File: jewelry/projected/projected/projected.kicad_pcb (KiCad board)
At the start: 2 copper layers, 28 x 28 mm, 29 parts, among them J4 Leds, U1 STM32F042K6U6, U2 MCP73812T-420I-OT, U3 PCA9306DCUR, U4 MCP1640BCH

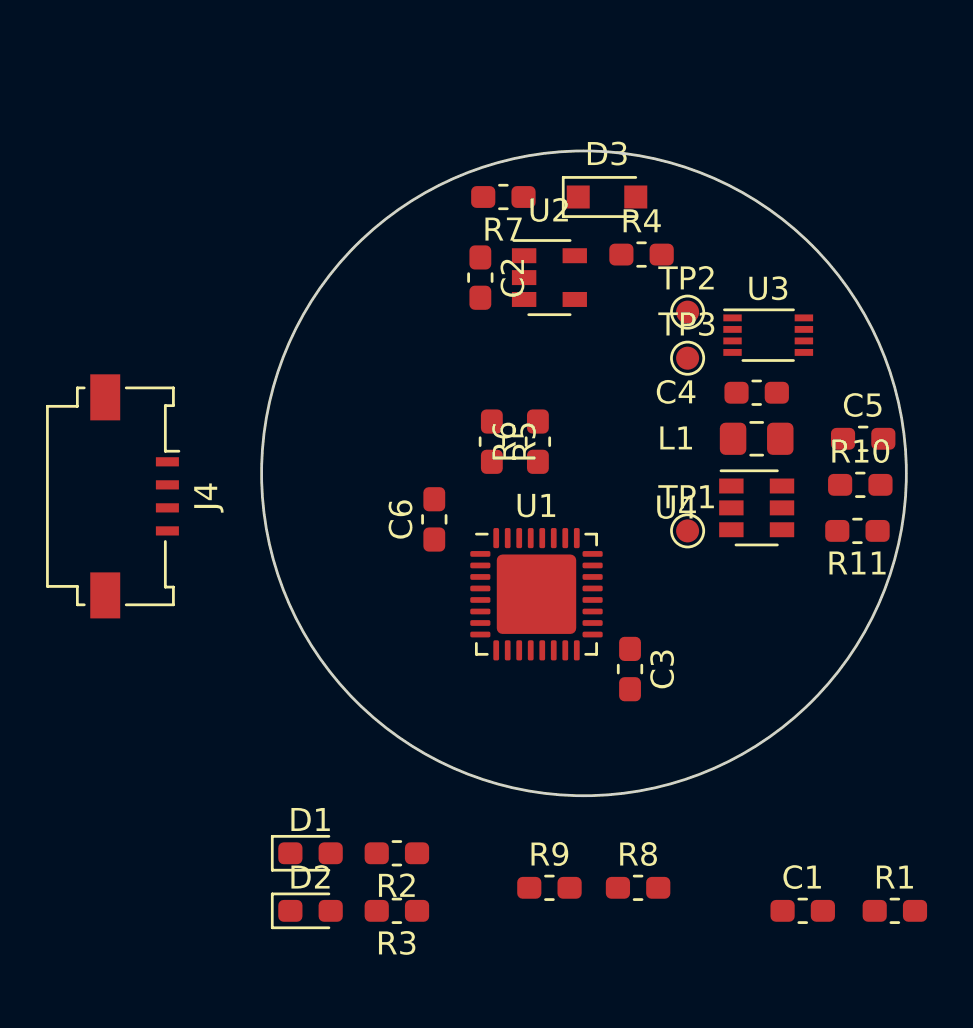
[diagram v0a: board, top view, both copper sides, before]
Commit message: projected: Try to fit accelerometer and mic
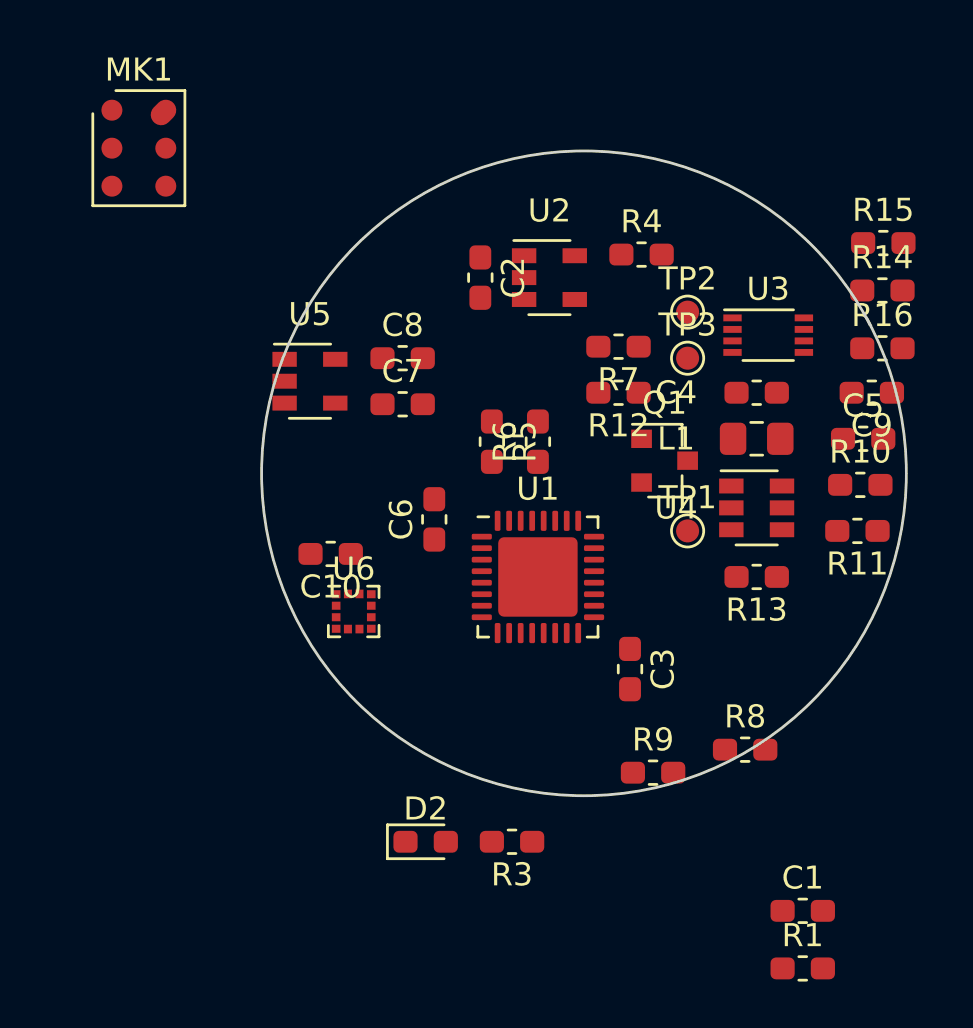
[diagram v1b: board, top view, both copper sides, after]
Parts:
- removed D1: LED, LED_SMD:LED_0603_1608Metric_Pad1.05x0.95mm_HandSolder
- removed D3: Z3V9, Diode_SMD:D_SOD-323_HandSoldering
- removed J4: Leds, Connector_FFC-FPC:Molex_200528-0040_1x04-1MP_P1.00mm_Horizontal
- removed R2: R, Resistor_SMD:R_0603_1608Metric_Pad1.05x0.95mm_HandSolder
- added C10: 1uF, Capacitor_SMD:C_0603_1608Metric_Pad1.05x0.95mm_HandSolder, F.Cu at (39.0, 53.5)
- added C7: 1uF, Capacitor_SMD:C_0603_1608Metric_Pad1.05x0.95mm_HandSolder, F.Cu at (42.1, 47.0)
- added C8: 1uF, Capacitor_SMD:C_0603_1608Metric_Pad1.05x0.95mm_HandSolder, F.Cu at (42.1, 45.0)
- added C9: 1uF, Capacitor_SMD:C_0603_1608Metric_Pad1.05x0.95mm_HandSolder, F.Cu at (62.5, 46.5)
- added MK1: MP45DT02, Sensor_Audio:ST_HLGA-6_3.76x4.72mm_P1.65mm, F.Cu at (30.7, 35.9)
- added Q1: BC847, Package_TO_SOT_SMD:SOT-23, F.Cu at (53.5, 49.5)
- added R12: 4k7, Resistor_SMD:R_0603_1608Metric_Pad1.05x0.95mm_HandSolder, F.Cu at (51.5, 46.5)
- added R13: 100k, Resistor_SMD:R_0603_1608Metric_Pad1.05x0.95mm_HandSolder, F.Cu at (57.5, 54.5)
- added R14: 100k, Resistor_SMD:R_0603_1608Metric_Pad1.05x0.95mm_HandSolder, F.Cu at (63.0, 42.1)
- added R15: 3k3, Resistor_SMD:R_0603_1608Metric_Pad1.05x0.95mm_HandSolder, F.Cu at (63.0, 40.0)
- added R16: 3k3, Resistor_SMD:R_0603_1608Metric_Pad1.05x0.95mm_HandSolder, F.Cu at (63.0, 44.6)
- added U5: TPS7A0533, Package_TO_SOT_SMD:SOT-23-5, F.Cu at (38.1, 46.0)
- added U6: LIS2DE12, Package_LGA:LGA-12_2x2mm_P0.5mm, F.Cu at (40.0, 56.0)
- R7: value R -> 4k7
- U1: value STM32F042K6U6 -> STM32L432KBU6
- moved R7 8.20 mm to (51.5, 44.5)
- moved R8 7.59 mm to (57.0, 62.0)
- moved R9 6.73 mm to (53.0, 63.0)
- moved D2 5.83 mm to (43.1, 66.0)
- moved R3 5.83 mm to (46.9, 66.0)
- moved R1 4.72 mm to (59.5, 71.5)
- moved U1 0.75 mm to (48.0, 54.5)
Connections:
- net /SPI1_MISO renamed Net-(U1-Pad12)
- net /USART2_RX renamed Net-(U1-Pad9)
- net /USB_NOE renamed /TOUCH_2
- net Net-(U1-Pad30) renamed /TOUCH_1
- net Net-(U1-Pad7) renamed /ANALOG-
- R1 pad 2: /TOUCH_SENSE -> Net-(R1-Pad2)
- R7 pad 1: VCC -> +BATT
- R7 pad 2: +BATT -> /LED_ENABLE
- TP1 pad 1: /LED_ENABLE -> Net-(Q1-Pad3)
- U1 pad 10: Net-(U1-Pad10) -> /BATT_SENSE
- U1 pad 14: /TOUCH_SENSE -> Net-(U1-Pad14)
- U1 pad 16: Net-(U1-Pad16) -> GND
- U1 pad 18: /MCO -> /LED_ENABLE
- U1 pad 19: /I2C1_SCL -> /I2C_SCL
- U1 pad 2: Net-(U1-Pad2) -> /LED_STATUS
- U1 pad 20: /I2C1_SDA -> /I2C_SDA
- U1 pad 26: /LED_STATUS -> /SAI_SCK
- U1 pad 27: /LED_ENABLE -> Net-(U1-Pad27)
- U1 pad 28: /LED_ONBOARD -> /SAI_SD
- U1 pad 32: Net-(U1-Pad32) -> GND
- U1 pad 6: /BATT_SENSE -> /ANALOG+
- U1 pad 8: /USART2_TX -> /ACCEL_INT
- U3 pad 7: +5V -> Net-(R14-Pad1)
- U3 pad 8: +5V -> Net-(R14-Pad1)
- U4 pad 3: /LED_ENABLE -> Net-(Q1-Pad3)

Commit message: projected: Layout nearly done
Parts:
- added BT1: LIR2450, Battery:BatteryHolder_Keystone_3008_1x2450, F.Cu at (72.9, 78.7)
- added C11: 1uF, Capacitor_SMD:C_0603_1608Metric_Pad1.05x0.95mm_HandSolder, F.Cu at (56.3, 59.6)
- added J1: TOUCH, Connector_PinHeader_1.27mm:PinHeader_1x03_P1.27mm_Vertical, F.Cu at (47.0, 62.7)
- added J3: DOCK, Connector_PinHeader_1.27mm:PinHeader_1x06_P1.27mm_Vertical, F.Cu at (37.3, 47.2)
- added J4: Leds, Connector_PinHeader_1.27mm:PinHeader_1x04_P1.27mm_Vertical, F.Cu at (60.7, 41.9)
- added J5: SWD, Connector_PinHeader_1.27mm:PinHeader_1x06_P1.27mm_Vertical, F.Cu at (43.4, 61.2)
- added J6: EXT, Connector_PinHeader_1.27mm:PinHeader_1x06_P1.27mm_Vertical, F.Cu at (43.2, 38.6)
- added R2: 1k, Resistor_SMD:R_0603_1608Metric_Pad1.05x0.95mm_HandSolder, F.Cu at (45.5, 58.2)
- R1: value R -> 1k
- moved MK1 33.4 mm to (53.1, 60.6), turned to 180 degrees
- moved R1 20.7 mm to (43.9, 57.9), turned to 90 degrees
- moved C1 16.5 mm to (47.0, 58.2), turned to 270 degrees
- moved D2 16.3 mm to (52.1, 52.3)
- moved C10 13.8 mm to (48.8, 43.7), turned to 270 degrees
- moved R3 13.0 mm to (52.1, 54.1), turned to 0 degrees
- moved R6 9.56 mm to (52.3, 57.1), turned to 0 degrees
- moved R5 9.10 mm to (49.8, 56.9)
- moved R9 8.37 mm to (57.4, 55.9)
- moved U5 8.14 mm to (46.0, 43.9)
- moved R8 7.72 mm to (59.9, 54.9), turned to 90 degrees
- moved R14 6.78 mm to (56.4, 40.4), turned to 180 degrees
- moved R16 6.57 mm to (56.4, 44.7), turned to 180 degrees
- moved U6 5.85 mm to (41.3, 50.3), turned to 180 degrees
- moved R15 5.49 mm to (58.9, 43.7), turned to 270 degrees
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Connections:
- C1 pad 1: Net-(C1-Pad1) -> /TOUCH_CS
- C1 pad 2: Net-(C1-Pad2) -> GND
- R1 pad 2: Net-(R1-Pad2) -> /TOUCH_1
- U1 pad 12: Net-(U1-Pad12) -> /LED_ENABLE
- U1 pad 18: /LED_ENABLE -> Net-(U1-Pad18)
- U1 pad 25: /TOUCH_2 -> Net-(U1-Pad25)
- U1 pad 27: Net-(U1-Pad27) -> /TOUCH_1
- U1 pad 29: Net-(U1-Pad29) -> /TOUCH_2
- U1 pad 30: /TOUCH_1 -> /TOUCH_CS
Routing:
- net +BATT: track 0.00 -> 37.4 mm, vias 0 -> 4
- net VCC: track 0.00 -> 22.7 mm
- net VBUS: track 0.00 -> 21.5 mm
- net +5V: track 0.00 -> 21.0 mm
- net /ANALOG+: track 0.00 -> 20.2 mm, vias 0 -> 2
- net /BOOT: track 0.00 -> 20.2 mm, vias 0 -> 1
- net /ANALOG-: track 0.00 -> 18.8 mm, vias 0 -> 2
- net /RESET: track 0.00 -> 18.1 mm, vias 0 -> 2
- net /I2C_SDA: track 0.00 -> 17.7 mm
- net /LED_DATA: track 0.00 -> 14.2 mm, vias 0 -> 2
- net /SAI_SCK: track 0.00 -> 13.6 mm, vias 0 -> 2
- net /I2C_SCL: track 0.00 -> 13.5 mm
- net /SAI_SD: track 0.00 -> 11.0 mm, vias 0 -> 2
- net /LED_CLK: track 0.00 -> 10.8 mm
- net /LED_ENABLE: track 0.00 -> 9.81 mm, vias 0 -> 2
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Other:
- board outline removed
- net class Default: via_dia 0.8 -> 0.6; via_drill 0.4 -> 0.3

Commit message: projected: Intial layout done
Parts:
- removed BT1: LIR2450, Battery:BatteryHolder_Keystone_3008_1x2450
- moved C10 2.90 mm to (50.2, 41.1), turned to 0 degrees
- moved C11 1.37 mm to (57.5, 59.1)
- moved R14 0.90 mm to (55.5, 40.5)
- moved C7 0.65 mm to (43.3, 43.3)
- moved MK1 0.54 mm to (53.5, 60.2), turned to 270 degrees
- moved R8 0.28 mm to (60.1, 55.1)
- moved J4 0.28 mm to (60.8, 41.7)
- moved C8 0.13 mm to (46.0, 41.4)
- moved U5 0.13 mm to (46.1, 43.9)
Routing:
- net VCC: track 22.7 -> 105.6 mm, vias 0 -> 10
- net GND: track 4.19 -> 47.3 mm, vias 0 -> 11
- net /BATT_SENSE: track 1.72 -> 21.0 mm, vias 0 -> 2
- net /ACCEL_INT: track 7.64 -> 9.60 mm, vias 1 -> 2
- net Net-(D2-Pad2): track 0.00 -> 1.78 mm
- net /SAI_SCK: track 13.6 -> 15.1 mm
- net /BOOT: track 20.2 -> 18.8 mm
- net /SAI_SD: track 11.0 -> 12.4 mm
- net VBUS: track 21.5 -> 20.4 mm, vias 0 -> 2
- net /RESET: track 18.1 -> 19.2 mm
- net /LED_CLK: track 10.8 -> 11.8 mm
- added copper zone on B.Cu, net GND
- added copper zone on F.Cu, net GND

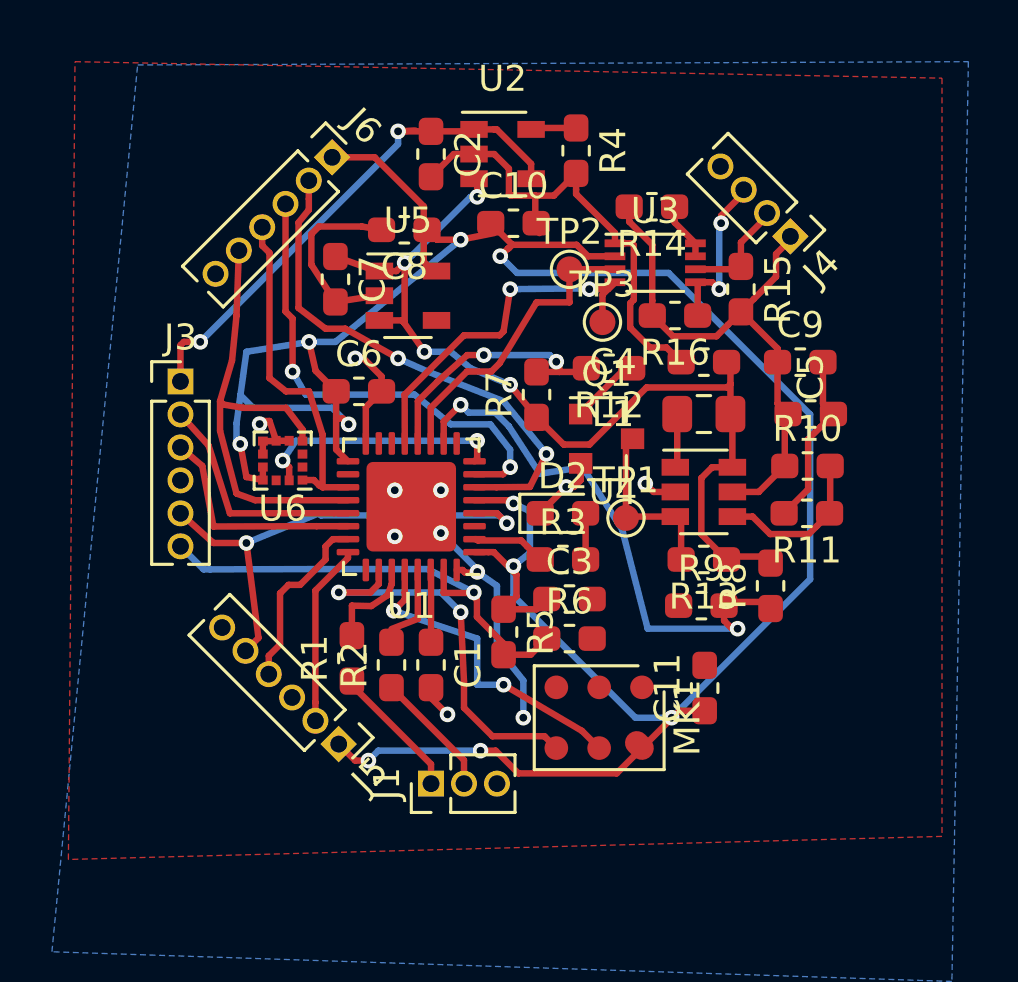
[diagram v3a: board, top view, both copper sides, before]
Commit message: projected: Start to add battery
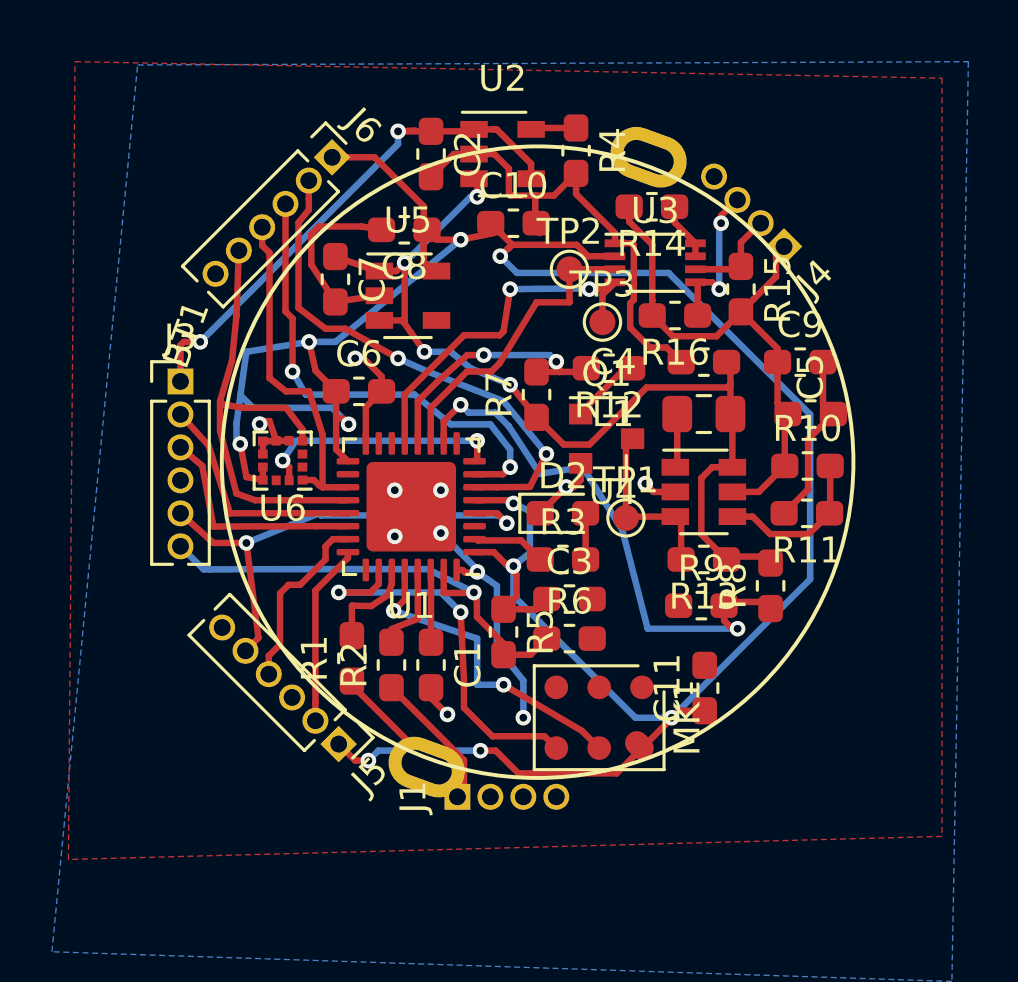
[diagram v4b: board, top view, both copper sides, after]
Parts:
- added BT1: LIR2450, projected:LIR2450-horizontal-pins, F.Cu at (51.1, 50.4)
- C3: value 100nF -> 1uF
- J1: footprint Connector_PinHeader_1.27mm:PinHeader_1x03_P1.27mm_Vertical -> projected:Pins_1x04_P1.27mm
- J3, J5, J6: footprint Connector_PinHeader_1.27mm:PinHeader_1x06_P1.27mm_Vertical -> projected:Pins_1x06_P1.27mm
- J4: footprint Connector_PinHeader_1.27mm:PinHeader_1x04_P1.27mm_Vertical -> projected:Pins_1x04_P1.27mm
- Q1: value BC847 -> BC847CL
- U4: value MCP1640BCH -> MCP1640BT-I/CHY‎
- U5: value TPS7A0533 -> TPS7A0533PDBVT
- U6: value LIS2DE12 -> LIS2DE12TR‎
- moved J1 1.14 mm to (48.0, 63.2)
- moved J4 0.46 mm to (60.6, 42.0)

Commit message: projected: Routing almost complete
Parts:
- TP1, TP2, TP3: footprint TestPoint:TestPoint_Pad_D1.0mm -> projected:TestPoint_Mini
- moved J1 0.77 mm to (48.8, 63.1)
- moved J4 0.54 mm to (61.0, 42.4)
- moved TP2 0.51 mm to (51.8, 42.9)
- moved R14 0.40 mm to (55.1, 40.6)
- moved J5 0.37 mm to (43.1, 61.1)
- moved TP1 0.13 mm to (54.6, 52.6)
- moved R1 0.13 mm to (43.9, 57.8)
- turned BT1 to 68 degrees
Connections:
- J1 pad 1: Net-(J1-Pad1) -> GND
- J1 pad 3: GND -> Net-(J1-Pad3)
- R1 pad 1: Net-(J1-Pad1) -> Net-(J1-Pad2)
- R2 pad 1: Net-(J1-Pad2) -> Net-(J1-Pad3)
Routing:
- net Net-(J1-Pad3): track 0.00 -> 7.51 mm
- net +BATT: track 37.2 -> 44.4 mm
- net Net-(J1-Pad1): track 5.21 -> 0.00 mm
- net Net-(J1-Pad2): track 4.85 -> 8.26 mm
- net GND: track 47.3 -> 50.6 mm, vias 11 -> 13
- net VCC: track 105.6 -> 107.0 mm, vias 10 -> 9
- net /LED_DATA_5V: track 6.26 -> 5.59 mm, vias 2 -> 1
- net /SAI_SCK: track 15.1 -> 14.6 mm
- net /LED_CLK: track 11.8 -> 12.3 mm

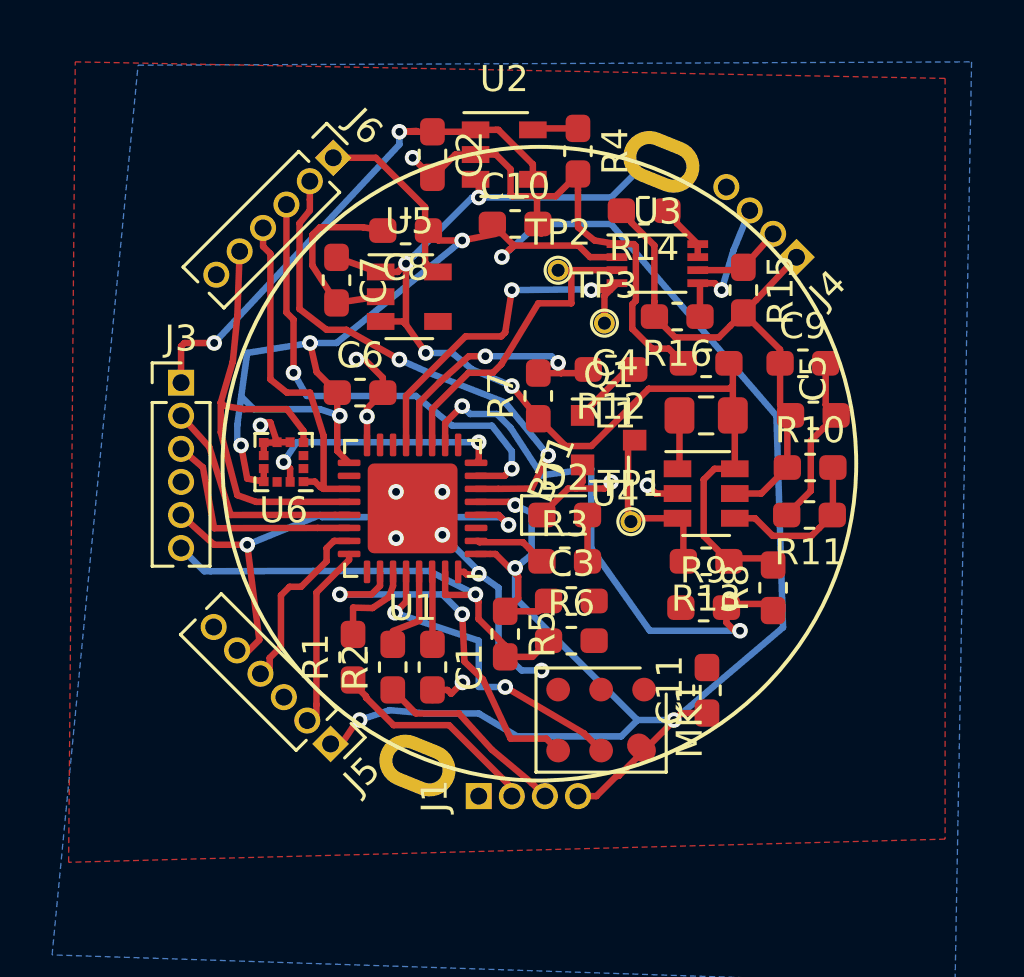
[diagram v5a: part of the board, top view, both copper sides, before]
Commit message: projected: Add routes connected
Still need to fix microphone footprint
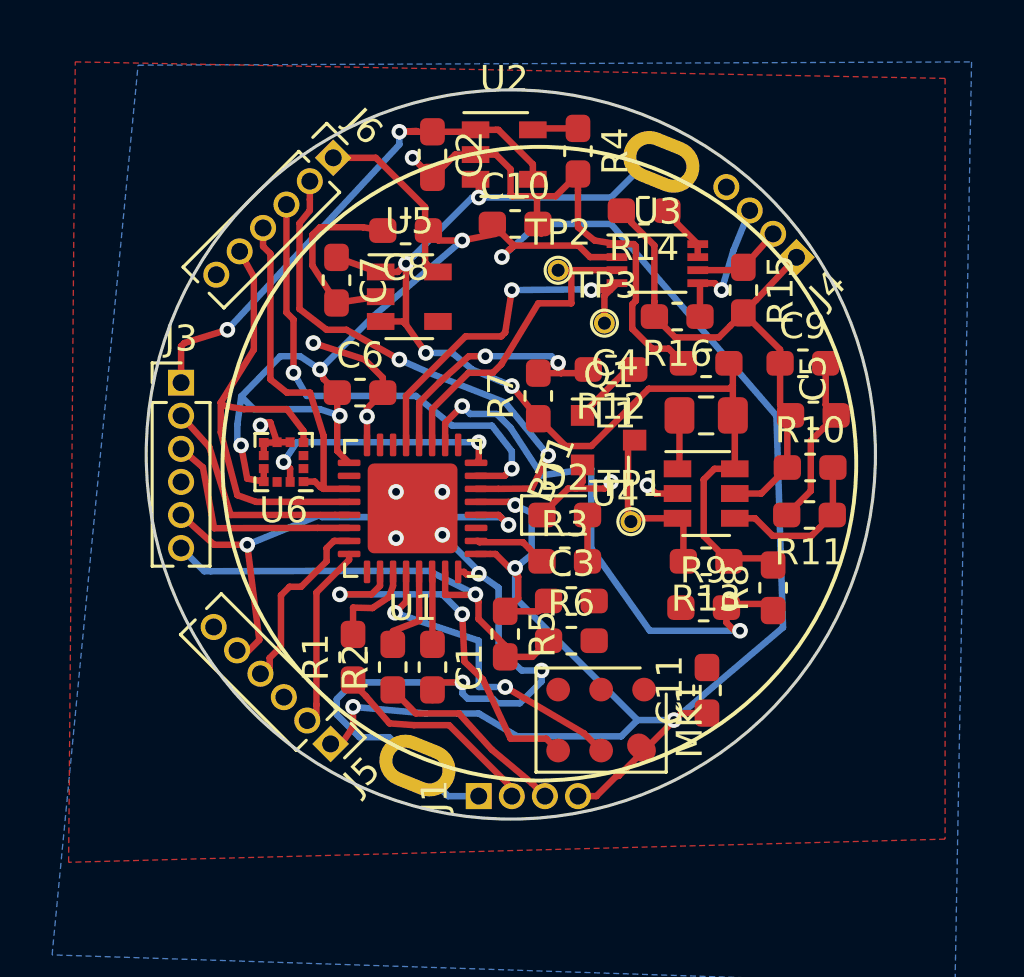
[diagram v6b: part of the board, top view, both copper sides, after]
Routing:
- net GND: track 50.6 -> 69.1 mm
- net VCC: track 107.0 -> 106.4 mm
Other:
- board outline added: 28 x 28 mm
